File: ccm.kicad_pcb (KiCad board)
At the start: 2 copper layers, 80.1 x 75.2 mm, 52 parts, among them J1 Conn_01x02_Socket, J10 Conn_01x02_Socket, J2 Conn_01x02_Socket, J3 Conn_01x02_Socket, J4 Conn_01x04_Socket, J5 Conn_01x02_Socket, J6 Conn_01x02_Socket, J7 Conn_01x02_Socket, J8 Conn_01x04_Socket, J9 Conn_01x02_Socket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

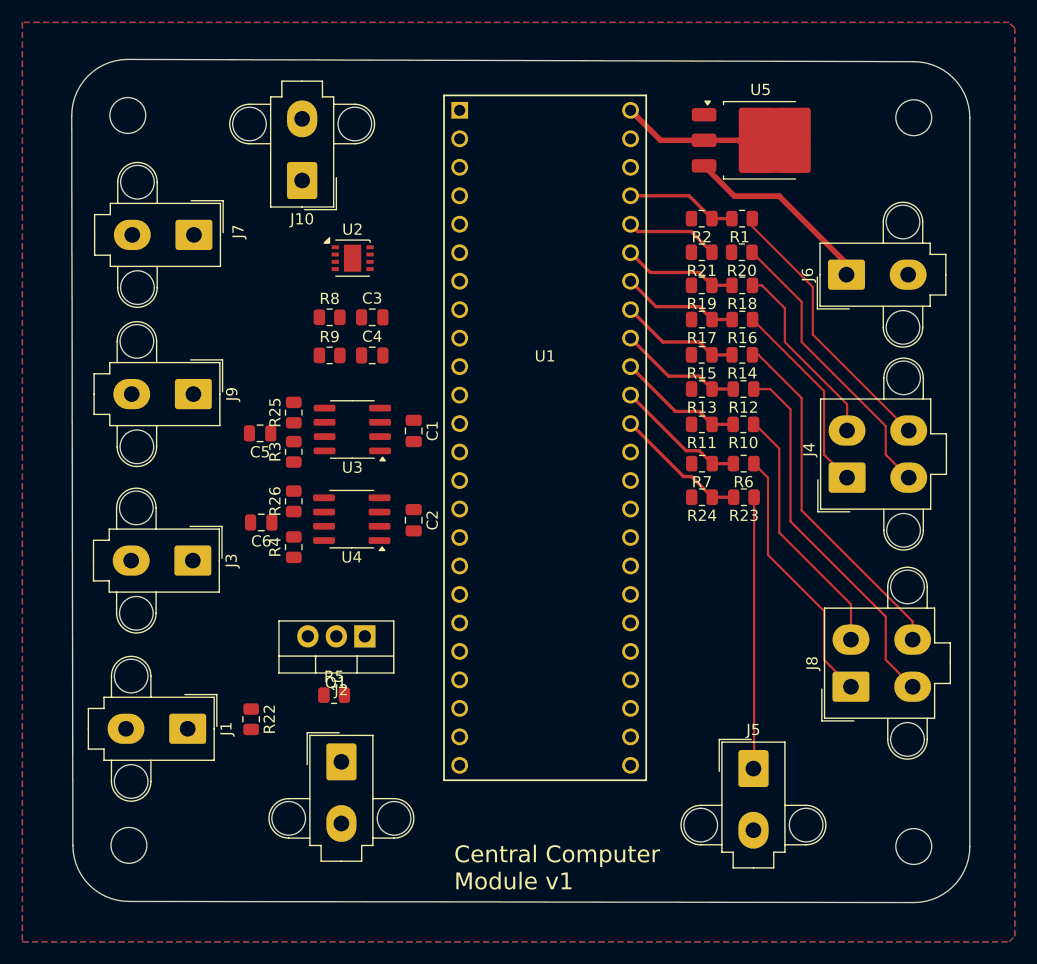
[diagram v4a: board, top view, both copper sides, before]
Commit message: finish new routing
Todo (serial resistors)
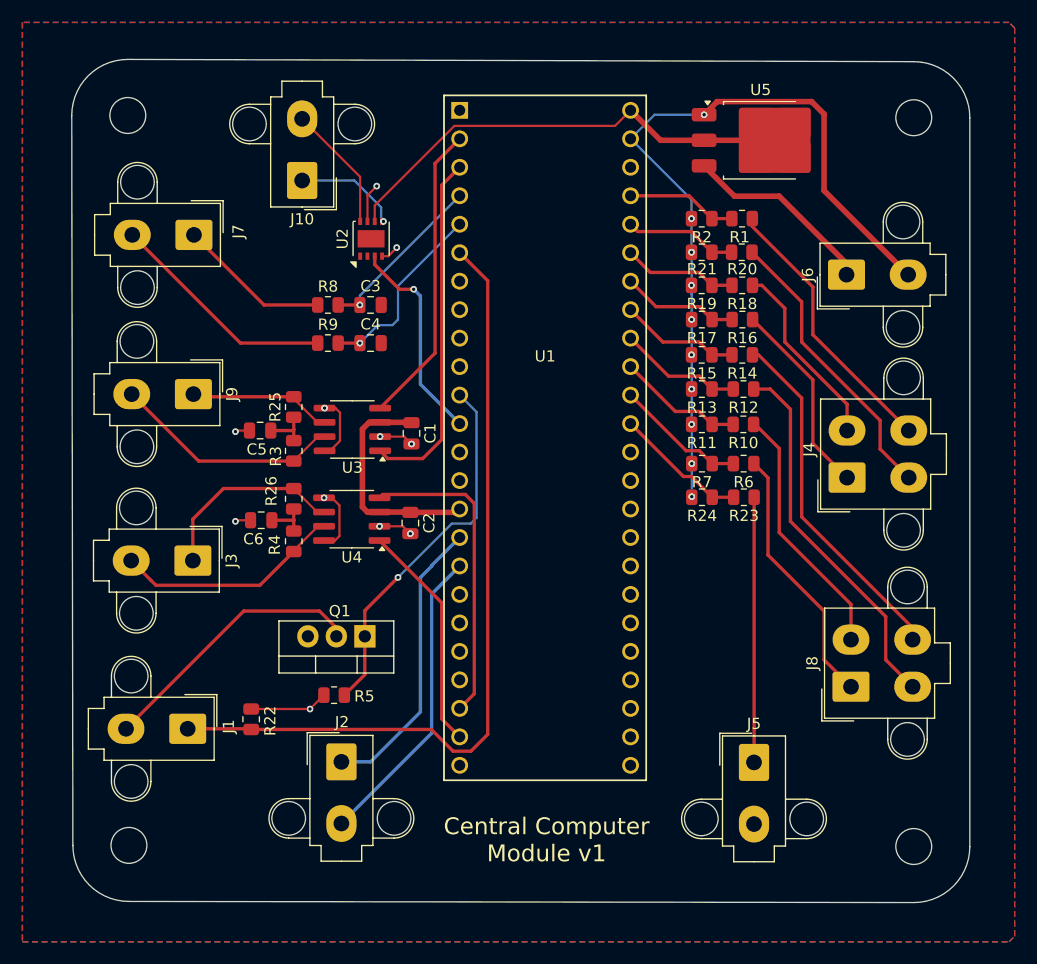
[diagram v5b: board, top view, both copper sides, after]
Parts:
- moved U2 2.39 mm to (135.6, 77.8), turned to 90 degrees
- moved R9 1.11 mm to (131.8, 87.1)
- moved C4 1.11 mm to (135.6, 87.1)
- moved R8 1.11 mm to (131.8, 83.7)
- moved C3 1.11 mm to (135.6, 83.7)
- moved J5 0.55 mm to (169.8, 124.5)
- moved R4 0.52 mm to (128.7, 104.8)
- moved R25 0.50 mm to (128.7, 92.8)
- moved C2 0.39 mm to (139.1, 103.2)
- moved C1 0.29 mm to (139.2, 95.2)
- moved C5 0.25 mm to (125.7, 94.9)
- moved R26 0.23 mm to (128.7, 101.0)
- moved C6 0.20 mm to (125.8, 102.9)
- moved R3 0.09 mm to (128.7, 96.7)
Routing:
- net GLV-: track 0.00 -> 104.5 mm, vias 0 -> 21
- net ready_to_drive_button: track 0.00 -> 72.2 mm
- net Net-(Q1-G): track 0.00 -> 33.2 mm, vias 0 -> 1
- net CAN_TX_1: track 0.00 -> 31.4 mm
- net +5V: track 12.9 -> 40.7 mm
- net CAN_RX_2: track 0.00 -> 27.7 mm
- net i2c_SDA: track 0.00 -> 27.3 mm
- net CAN_RX_1: track 0.00 -> 27.0 mm
- net i2c_SCL: track 0.00 -> 25.9 mm
- net brake_light: track 0.00 -> 24.5 mm
- net CANH_1: track 0.00 -> 20.7 mm
- net +3.3V: track 0.00 -> 20.6 mm
- net PWM_in_2: track 0.00 -> 20.5 mm
- net CAN_TX_2: track 0.00 -> 20.5 mm
- net CANH_2: track 0.00 -> 20.3 mm
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
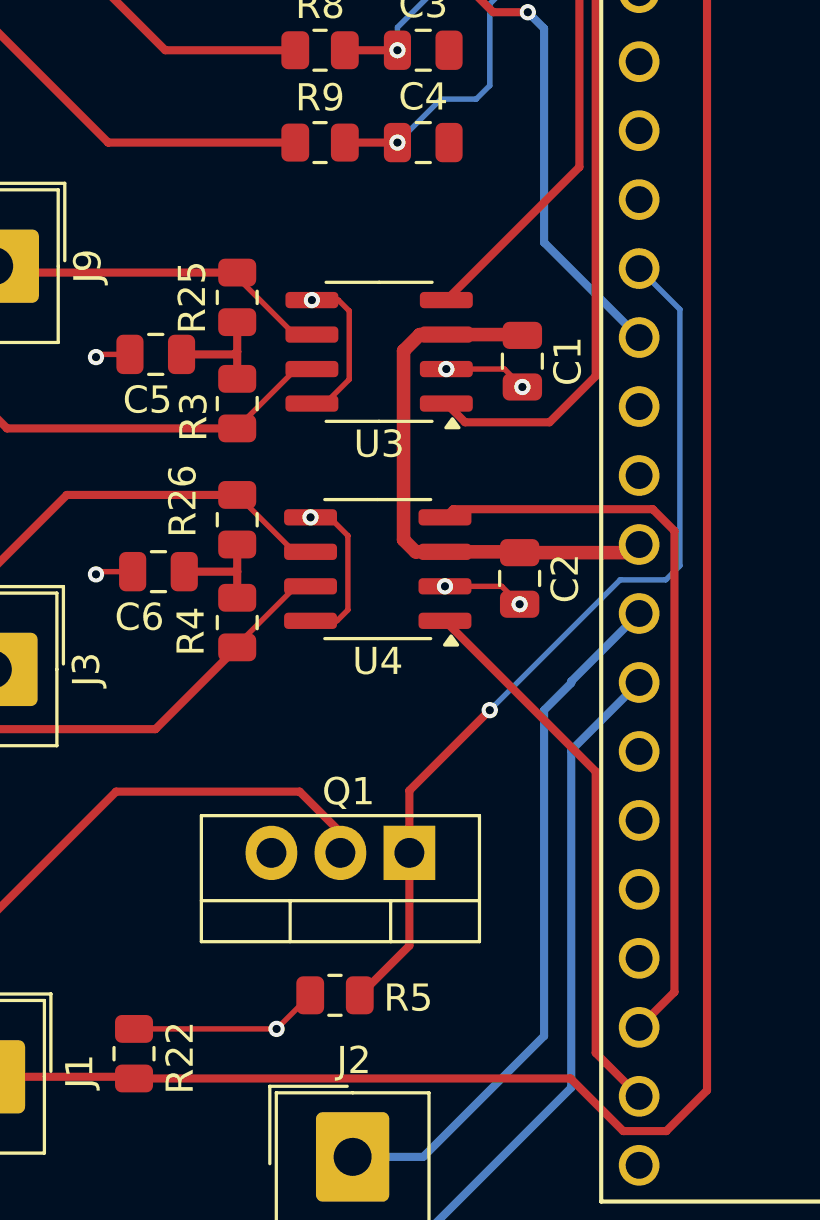
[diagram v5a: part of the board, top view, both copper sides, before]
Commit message: added serial resistors to CAN tranciever
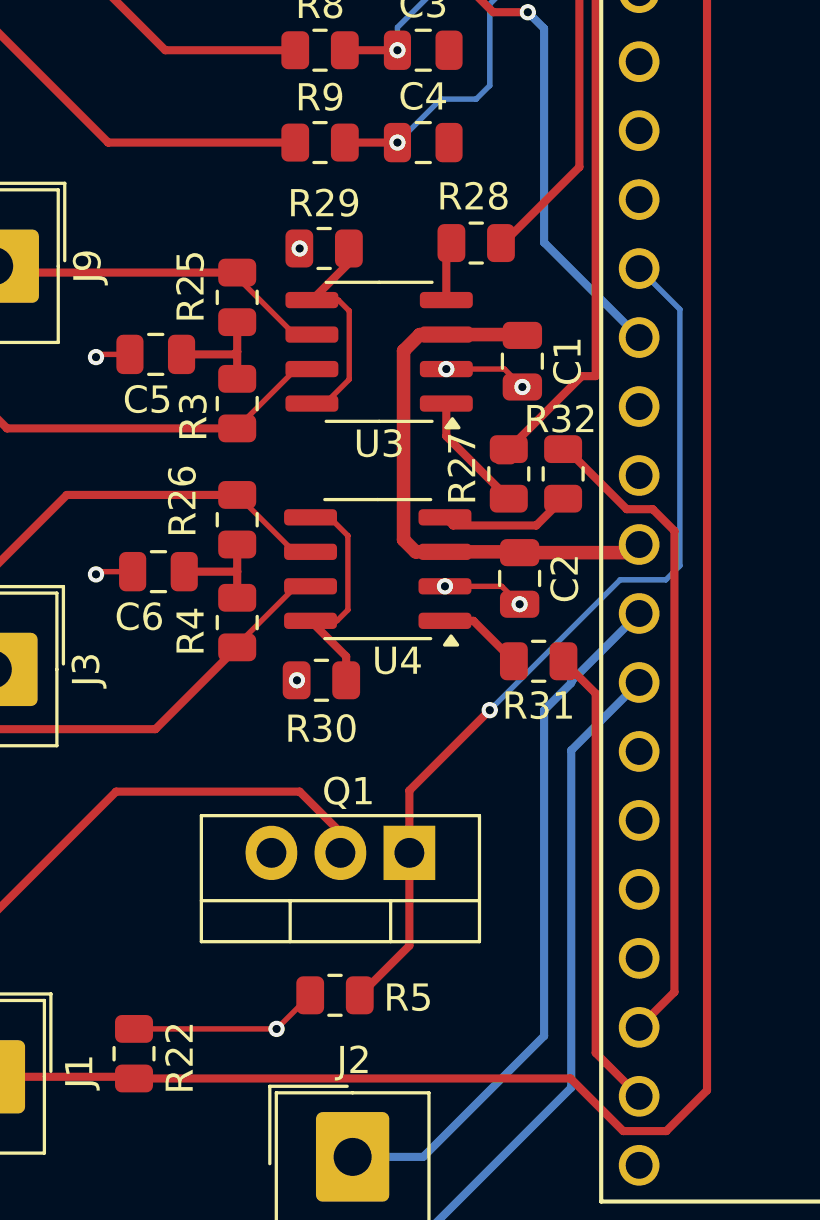
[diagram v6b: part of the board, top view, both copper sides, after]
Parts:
- added R27: 60, Resistor_SMD:R_0805_2012Metric, F.Cu at (138.7, 99.3)
- added R28: 60, Resistor_SMD:R_0805_2012Metric, F.Cu at (137.5, 90.8)
- added R29: 60, Resistor_SMD:R_0805_2012Metric, F.Cu at (131.9, 91.0)
- added R30: 60, Resistor_SMD:R_0805_2012Metric, F.Cu at (131.8, 106.9)
- added R31: 60, Resistor_SMD:R_0805_2012Metric, F.Cu at (139.8, 106.2)
- added R32: 60, Resistor_SMD:R_0805_2012Metric, F.Cu at (140.7, 99.3)
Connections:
- U3 pad 1: CAN_TX_1 -> Net-(U3-D)
- U3 pad 4: CAN_RX_1 -> Net-(U3-R)
- U3 pad 5: GLV- -> Net-(U3-Rs)
- U3 pad 8: GLV- -> Net-(U3-Rs)
- U4 pad 1: CAN_TX_2 -> Net-(U4-D)
- U4 pad 4: CAN_RX_2 -> Net-(U4-R)
- U4 pad 5: GLV- -> Net-(U4-Rs)
- U4 pad 8: GLV- -> Net-(U4-Rs)
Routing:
- net GLV-: track 104.5 -> 92.8 mm
- net Net-(U4-Rs): track 0.00 -> 8.66 mm
- net Net-(U3-Rs): track 0.00 -> 8.27 mm
- net Net-(U4-R): track 0.00 -> 4.88 mm
- net Net-(U3-D): track 0.00 -> 4.46 mm
- net CAN_RX_2: track 27.7 -> 24.2 mm
- net CAN_TX_2: track 20.5 -> 17.2 mm
- net Net-(U4-D): track 0.00 -> 3.15 mm
- net CAN_RX_1: track 27.0 -> 24.1 mm
- net Net-(U3-R): track 0.00 -> 2.18 mm
- net CAN_TX_1: track 31.4 -> 29.7 mm
